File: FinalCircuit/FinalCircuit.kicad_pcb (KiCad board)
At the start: 2 copper layers, 171.3 x 89.2 mm, 59 parts, among them J1 Conn_02x20_Odd_Even, J2 Conn_02x06_Odd_Even, J3 Conn_01x06, U1 LM6172, U10 CD4066BE, U11 CD4066BE, U2 OPA2277, U3 MCP3008, U4 MCP4921, U5 CD4066BE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

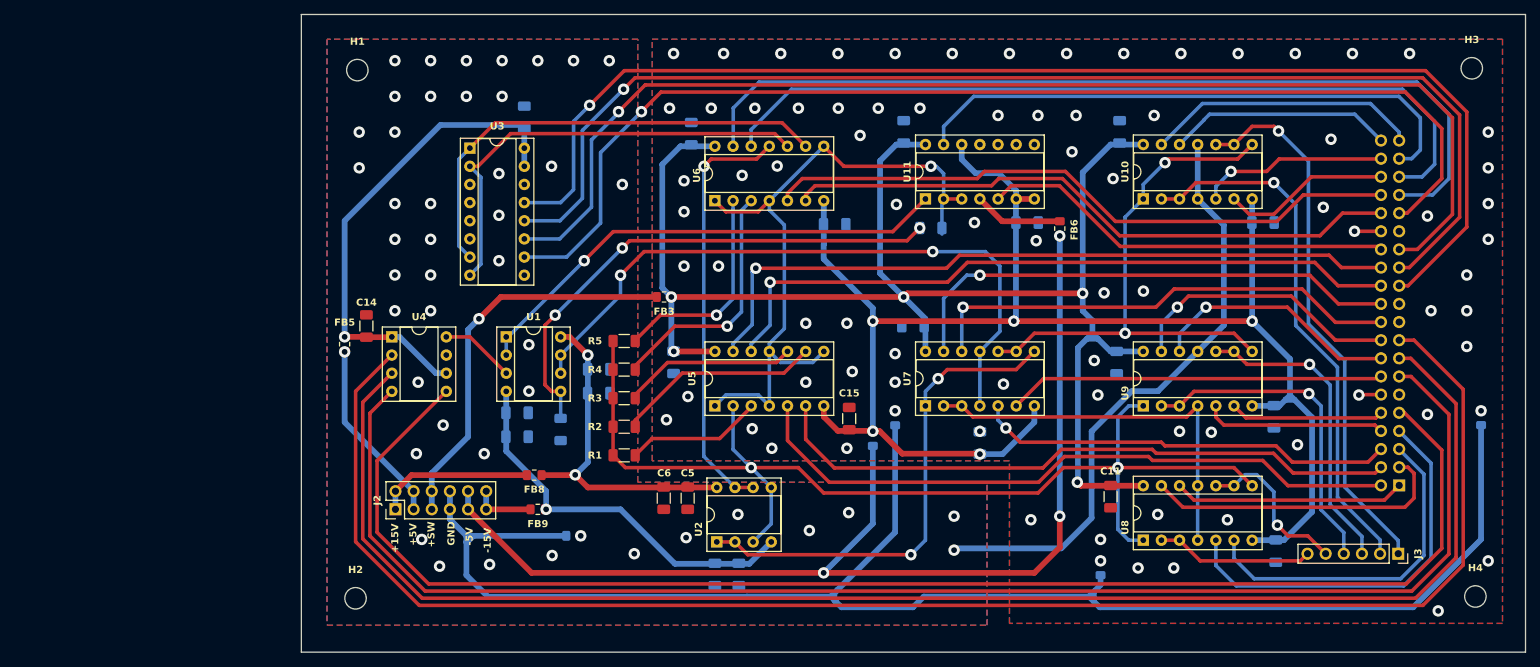
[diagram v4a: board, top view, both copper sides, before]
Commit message: Stage 2 verification done. Holes and connectors aligned. Final verification at PCB Lab left.
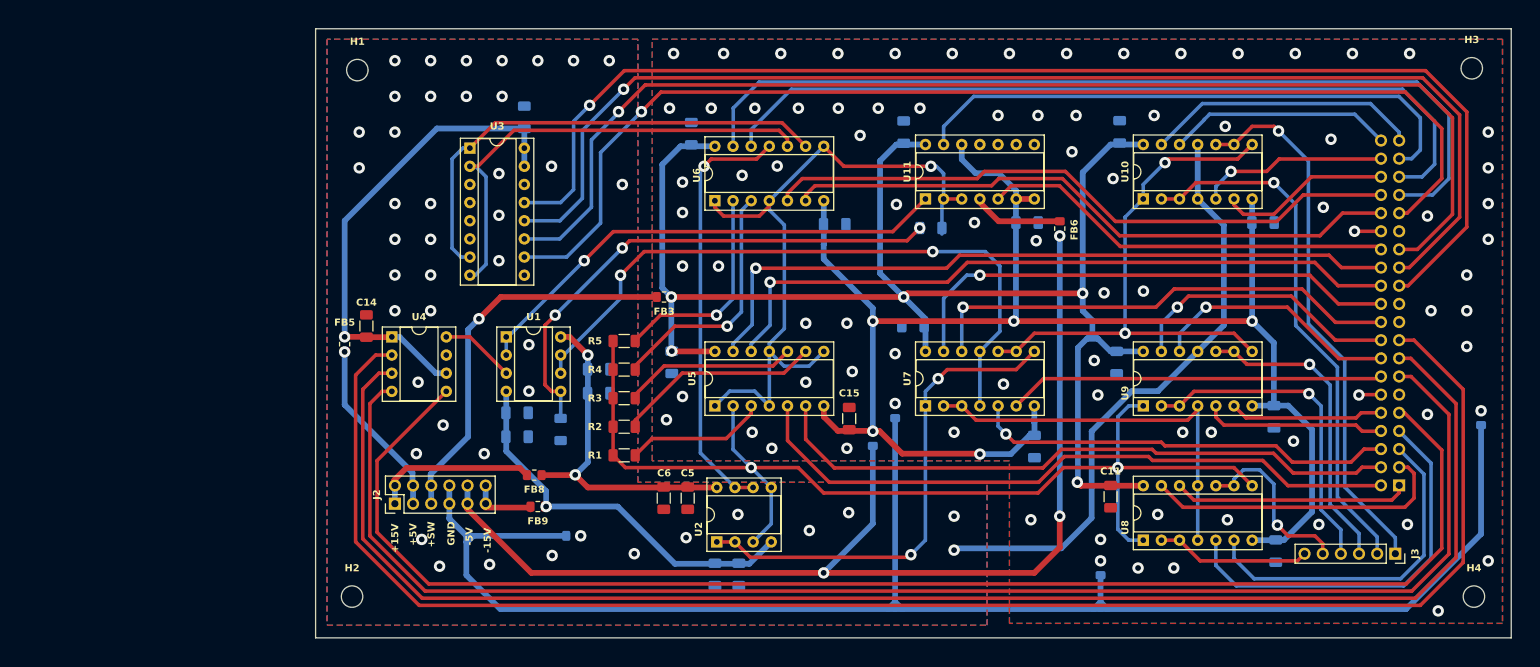
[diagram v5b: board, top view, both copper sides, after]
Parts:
- moved C10 7.65 mm to (189.5, 89.0), turned to -90 degrees
- moved FB1 1.00 mm to (170.0, 84.0)
- moved J2 0.79 mm to (100.0, 97.0)
- moved H2 0.54 mm to (94.0, 110.0)
- moved J3 0.41 mm to (240.0, 104.0)
- moved FB9 0.39 mm to (120.0, 97.4)
- moved C16 0.25 mm to (138.8, 77.2)
- moved H4 0.21 mm to (251.0, 110.0)
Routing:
- net /S8out: track 63.6 -> 66.1 mm
- net /Main: track 97.4 -> 99.7 mm
- net /Hz2: track 23.0 -> 25.2 mm
- net /S7out: track 66.3 -> 68.4 mm
- net /-5VD: track 222.4 -> 220.6 mm
- net /PowerGND: track 227.9 -> 229.6 mm
- net /+15V: track 21.9 -> 23.0 mm
- net /DAC_CSbar: track 225.7 -> 226.8 mm
- net /SCK: track 215.8 -> 216.9 mm
- net /+5V: track 26.0 -> 25.2 mm
- net /SDI: track 206.5 -> 207.3 mm
- net /S9out: track 55.6 -> 56.4 mm
- net /Control_Hz2B: track 32.4 -> 33.0 mm
- net /S2out: track 19.2 -> 19.7 mm
- net GNDD: vias 82 -> 84
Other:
- board size 171.3 x 89.2 mm -> 167.3 x 85.2 mm

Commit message: Some more alignments completed. Verification done again. Final order left.
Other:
- board text added: "EDL 2024"
- board text added: "MON-08: An FPGA Based Instrument for RRAM Characterization"
- board text added: "Team- Debasish, Harshit, Shreyas, Varad"
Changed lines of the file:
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@@
 		(tags "mounting hole 3mm no annular")
 		(property "Reference" "H1"
-			(at 0 -4 0)
+			(at 4.458 0.078 0)
 			(layer "F.SilkS")
 			(effects
@@
 		(tags "mounting hole 3mm no annular")
 		(property "Reference" "H3"
-			(at 0 -4 0)
+			(at -4.898 0.132 0)
 			(layer "F.SilkS")
 			(effects
@@
 		(layer "Edge.Cuts")
 	)
+	(gr_text "EDL 2024"
+		(at 119.8 111 0)
+		(layer "B.SilkS")
+		(effects
+			(font
+				(size 2 2)
+				(thickness 0.2)
+			)
+			(justify left bottom mirror)
+		)
+	)
 	(gr_text "+SW"
 		(at 105.664 103.124 90)
@@
 		)
 	)
+	(gr_text "Team- Debasish, Harshit, Shreyas, Varad"
+		(at 144 111 0)
+		(layer "F.SilkS")
+		(effects
+			(font
+				(size 2 2)
+				(thickness 0.2)
+			)
+			(justify left bottom)
+		)
+	)
 	(gr_text "-15V"
 		(at 113.538 103.891 90)
@@
 				(thickness 0.2)
 				(bold yes)
+			)
+			(justify left bottom)
+		)
+	)
+	(gr_text "MON-08: An FPGA Based Instrument for RRAM Characterization"
+		(at 121 38 0)
+		(layer "F.SilkS")
+		(effects
+			(font
+				(size 2 2)
+				(thickness 0.2)
+				(bold yes)

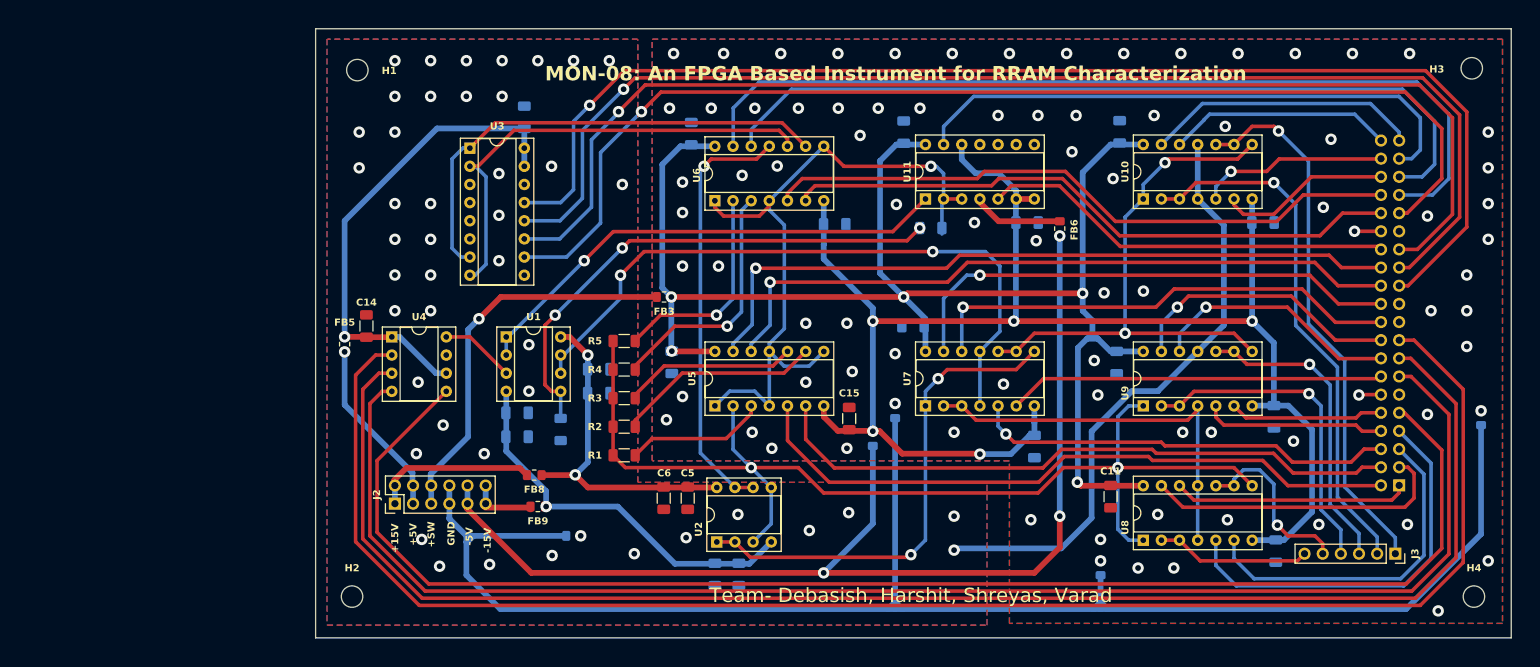
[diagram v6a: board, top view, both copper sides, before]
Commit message: Some minor silkscreen changes and constraints.
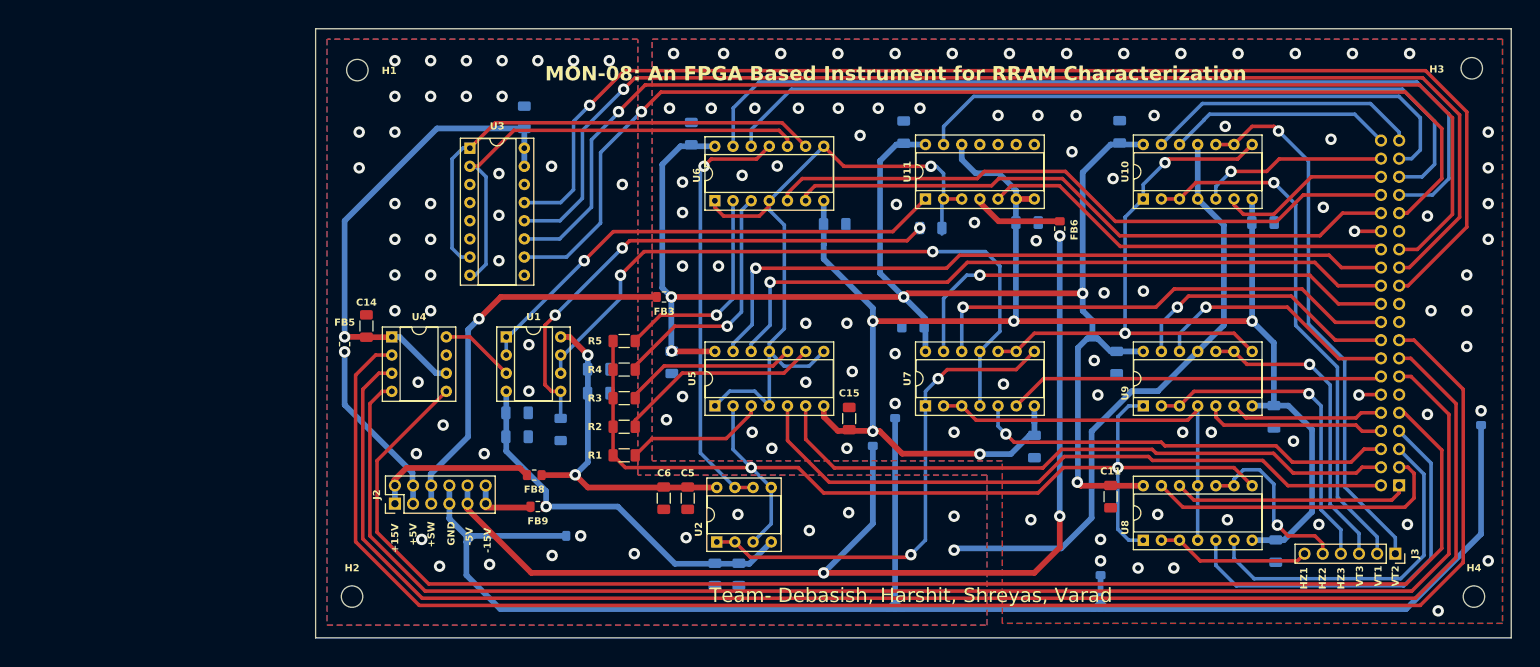
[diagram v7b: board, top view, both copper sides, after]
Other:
- board text added: "1"
- board text added: "11 (VCC)"
- board text added: "12 (DGND)"
- board text added: "2"
- board text added: "29 (3.3V)"
- board text added: "30 (DGND)"
- board text added: "40"
- board text added: "HZ1"
- board text added: "HZ2"
- board text added: "HZ3"
- board text added: "VT1"
- board text added: "VT2"
- board text added: "VT3"
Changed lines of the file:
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@@
 		(layer "Edge.Cuts")
 	)
+	(gr_text "11 (VCC)"
+		(at 249.4 82.4 0)
+		(layer "B.SilkS")
+		(effects
+			(font
+				(size 1 1)
+				(thickness 0.2)
+				(bold yes)
+			)
+			(justify left bottom mirror)
+		)
+	)
+	(gr_text "12 (DGND)"
+		(at 236.2 82.4 0)
+		(layer "B.SilkS")
+		(effects
+			(font
+				(size 1 1)
+				(thickness 0.2)
+				(bold yes)
+			)
+			(justify left bottom mirror)
+		)
+	)
 	(gr_text "EDL 2024"
 		(at 119.8 111 0)
@@
 		)
 	)
+	(gr_text "2"
+		(at 236 95 0)
+		(layer "B.SilkS")
+		(effects
+			(font
+				(size 1 1)
+				(thickness 0.2)
+				(bold yes)
+			)
+			(justify left bottom mirror)
+		)
+	)
+	(gr_text "29 (3.3V)"
+		(at 249.8 59.6 0)
+		(layer "B.SilkS")
+		(effects
+			(font
+				(size 1 1)
+				(thickness 0.2)
+				(bold yes)
+			)
+			(justify left bottom mirror)
+		)
+	)
+	(gr_text "1"
+		(at 244 95 0)
+		(layer "B.SilkS")
+		(effects
+			(font
+				(size 1 1)
+				(thickness 0.2)
+				(bold yes)
+			)
+			(justify left bottom mirror)
+		)
+	)
+	(gr_text "30 (DGND)"
+		(at 236 59.4 0)
+		(layer "B.SilkS")
+		(effects
+			(font
+				(size 1 1)
+				(thickness 0.2)
+				(bold yes)
+			)
+			(justify left bottom mirror)
+		)
+	)
+	(gr_text "40"
+		(at 236 47 0)
+		(layer "B.SilkS")
+		(effects
+			(font
+				(size 1 1)
+				(thickness 0.2)
+				(bold yes)
+			)
+			(justify left bottom mirror)
+		)
+	)
+	(gr_text "HZ3"
+		(at 233 109 90)
+		(layer "F.SilkS")
+		(effects
+			(font
+				(size 1 1)
+				(thickness 0.2)
+				(bold yes)
+			)
+			(justify left bottom)
+		)
+	)
+	(gr_text "VT1"
+		(at 238.2 108.6 90)
+		(layer "F.SilkS")
+		(effects
+			(font
+				(size 1 1)
+				(thickness 0.2)
+				(bold yes)
+			)
+			(justify left bottom)
+		)
+	)
 	(gr_text "+SW"
 		(at 105.664 103.124 90)
@@
 		)
 	)
+	(gr_text "VT3"
+		(at 235.6 108.6 90)
+		(layer "F.SilkS")
+		(effects
+			(font
+				(size 1 1)
+				(thickness 0.2)
+				(bold yes)
+			)
+			(justify left bottom)
+		)
+	)
+	(gr_text "HZ1"
+		(at 227.8 109 90)
+		(layer "F.SilkS")
+		(effects
+			(font
+				(size 1 1)
+				(thickness 0.2)
+				(bold yes)
+			)
+			(justify left bottom)
+		)
+	)
 	(gr_text "-15V"
 		(at 113.538 103.891 90)
@@
 		)
 	)
+	(gr_text "HZ2"
+		(at 230.4 109 90)
+		(layer "F.SilkS")
+		(effects
+			(font
+				(size 1 1)
+				(thickness 0.2)
+				(bold yes)
+			)
+			(justify left bottom)
+		)
+	)
+	(gr_text "VT2"
+		(at 240.6 108.6 90)
+		(layer "F.SilkS")
+		(effects
+			(font
+				(size 1 1)
+				(thickness 0.2)
+				(bold yes)
+			)
+			(justify left bottom)
+		)
+	)
 	(gr_text "MON-08: An FPGA Based Instrument for RRAM Characterization"
 		(at 121 38 0)
@@
 		(polygon
 			(pts
-				(xy 134 32) (xy 90.5 32) (xy 90.5 114) (xy 182.864 114) (xy 182.864 94) (xy 134 94)
+				(xy 134 32) (xy 90.5 32) (xy 90.5 114) (xy 182.864 114) (xy 182.864 93) (xy 134 93)
 			)
 		)
@@
 		(polygon
 			(pts
-				(xy 255 113.75) (xy 186 113.75) (xy 186 91) (xy 136 91) (xy 136 32) (xy 255 32)
+				(xy 255 113.75) (xy 185 113.75) (xy 185 91) (xy 136 91) (xy 136 32) (xy 255 32)
 			)
 		)
